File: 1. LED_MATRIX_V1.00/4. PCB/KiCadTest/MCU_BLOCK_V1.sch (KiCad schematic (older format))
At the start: 5 parts, among them U1 ATmega328P-AU, Y1 16 MHz

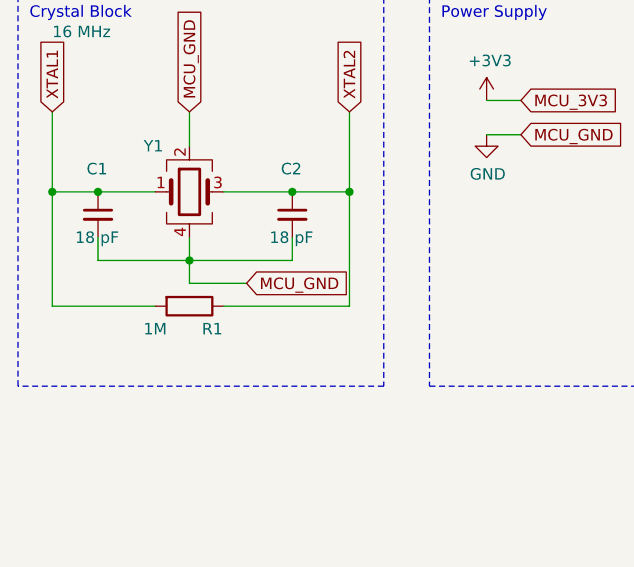
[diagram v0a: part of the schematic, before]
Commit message: Crystal complete_starting reset circuit
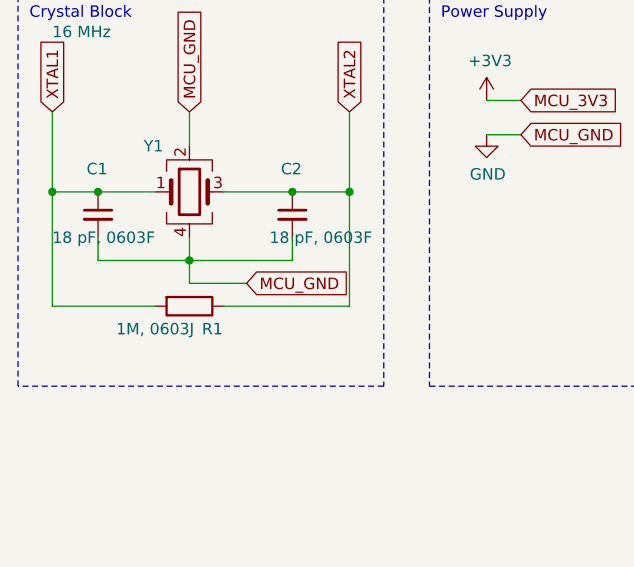
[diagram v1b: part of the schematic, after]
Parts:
- C1, C2: value 18 pF -> 18 pF, 0603F; footprint (none) -> Capacitor_SMD:C_0603_1608Metric
- R1: value 1M -> 1M, 0603J; footprint (none) -> Resistor_SMD:R_0603_1608Metric; Part Number (none) -> CRCW06031M00JKEA
- Y1: Part Number (none) -> TSX-3225 16.0000MF09Z-AC0
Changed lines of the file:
@@
 EESchema Schematic File Version 4
+LIBS:MCU_BLOCK_V1-cache
 EELAYER 29 0
 EELAYER END
@@
 F 2 "Oscillator:Oscillator_SMD_SeikoEpson_SG8002CE-4Pin_3.2x2.5mm_HandSoldering" H 1350 1400 50  0001 C CNN
 F 3 "" H 1350 1400 50  0001 C CNN
+F 4 "TSX-3225 16.0000MF09Z-AC0" H 1350 1400 50  0001 C CNN "Part Number"
 	1    1350 1400
 	1    0    0    -1
@@
 P 1350 1900
 F 0 "R1" V 1450 2000 50  0000 C CNN
-F 1 "1M" V 1450 1750 50  0000 C CNN
-F 2 "" V 1280 1900 50  0001 C CNN
+F 1 "1M, 0603J" V 1450 1750 50  0000 C CNN
+F 2 "Resistor_SMD:R_0603_1608Metric" V 1280 1900 50  0001 C CNN
 F 3 "~" H 1350 1900 50  0001 C CNN
+F 4 "CRCW06031M00JKEA" V 1350 1900 50  0001 C CNN "Part Number"
 	1    1350 1900
 	0    1    1    0
@@
 P 950 1500
 F 0 "C1" H 900 1700 50  0000 L CNN
-F 1 "18 pF" H 850 1400 50  0000 L CNN
-F 2 "" H 950 1500 50  0001 C CNN
+F 1 "18 pF, 0603F" H 750 1400 50  0000 L CNN
+F 2 "Capacitor_SMD:C_0603_1608Metric" H 950 1500 50  0001 C CNN
 F 3 "~" H 950 1500 50  0001 C CNN
 	1    950  1500
@@
 P 1800 1500
 F 0 "C2" H 1750 1700 50  0000 L CNN
-F 1 "18 pF" H 1700 1400 50  0000 L CNN
-F 2 "" H 1800 1500 50  0001 C CNN
+F 1 "18 pF, 0603F" H 1700 1400 50  0000 L CNN
+F 2 "Capacitor_SMD:C_0603_1608Metric" H 1800 1500 50  0001 C CNN
 F 3 "~" H 1800 1500 50  0001 C CNN
 	1    1800 1500

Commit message: Crystal complete_reset in progress
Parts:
- added C3: 0.1 uF, 0603J, Capacitor_SMD:C_0201_0603Metric, symbol Device:C
- added R2: 10 K, 0603J, Resistor_SMD:R_0201_0603Metric, symbol Device:R
- C1, C2: Part Number (none) -> VJ0603A180FXACW1BC
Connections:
- net +3V3: now also R2.1
- net GND: now also C3.2
- net RESET: now reaches U1.29 (~RESET~/PC6)
- net RESET: now also C3.1, R2.2
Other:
- note added: "Reset Block"
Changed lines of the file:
@@
 F 2 "Capacitor_SMD:C_0603_1608Metric" H 950 1500 50  0001 C CNN
 F 3 "~" H 950 1500 50  0001 C CNN
+F 4 "VJ0603A180FXACW1BC" H 950 1500 50  0001 C CNN "Part Number"
 	1    950  1500
 	1    0    0    -1
@@
 P 1800 1500
 F 0 "C2" H 1750 1700 50  0000 L CNN
-F 1 "18 pF, 0603F" H 1700 1400 50  0000 L CNN
+F 1 "18 pF, 0603F" H 1550 1400 50  0000 L CNN
 F 2 "Capacitor_SMD:C_0603_1608Metric" H 1800 1500 50  0001 C CNN
 F 3 "~" H 1800 1500 50  0001 C CNN
+F 4 "VJ0603A180FXACW1BC" H 1800 1500 50  0001 C CNN "Part Number"
 	1    1800 1500
 	1    0    0    -1
@@
 Text GLabel 5550 1850 1    50   Input ~ 0
 MCU_3V3
-Text GLabel 2800 1150 2    50   Input ~ 0
-MCU_GND
 Text GLabel 5550 5200 3    50   Input ~ 0
 MCU_GND
@@
 Wire Wire Line
 	5550 5200 5550 5050
+$Comp
+L Device:R R2
+U 1 1 5D504F89
+P 1200 2800
+F 0 "R2" H 1270 2846 50  0000 L CNN
+F 1 "10 K, 0603J" H 1270 2755 50  0000 L CNN
+F 2 "Resistor_SMD:R_0201_0603Metric" V 1130 2800 50  0001 C CNN
+F 3 "~" H 1200 2800 50  0001 C CNN
+F 4 "" H 1200 2800 50  0001 C CNN "Part Number"
+	1    1200 2800
+	1    0    0    -1
+$EndComp
+$Comp
+L Device:C C3
+U 1 1 5D5066E7
+P 1200 3200
+F 0 "C3" H 1315 3246 50  0000 L CNN
+F 1 "0.1 uF, 0603J" H 1200 3100 50  0000 L CNN
+F 2 "Capacitor_SMD:C_0201_0603Metric" H 1238 3050 50  0001 C CNN
+F 3 "~" H 1200 3200 50  0001 C CNN
+F 4 "" H 1200 3200 50  0001 C CNN "Part Number"
+	1    1200 3200
+	1    0    0    -1
+$EndComp
+Text GLabel 1200 2550 0    50   Input ~ 0
+MCU_3V3
+Text GLabel 2800 1150 2    50   Input ~ 0
+MCU_GND
+Text GLabel 1200 3450 0    50   Input ~ 0
+MCU_GND
+Wire Wire Line
+	1200 2550 1200 2650
+Wire Wire Line
+	1200 2950 1200 3000
+Wire Wire Line
+	1200 3350 1200 3450
+Text GLabel 1350 3000 2    50   Input ~ 0
+RESET
+Wire Wire Line
+	1350 3000 1200 3000
+Connection ~ 1200 3000
+Wire Wire Line
+	1200 3000 1200 3050
+Text GLabel 6350 3850 2    50   Input ~ 0
+RESET
+Wire Wire Line
+	6150 3850 6350 3850
+Wire Notes Line
+	600  3600 1750 3600
+Wire Notes Line
+	1750 3600 1750 2300
+Wire Notes Line
+	1750 2300 600  2300
+Wire Notes Line
+	600  2300 600  3600
+Text Notes 650  2400 0    50   ~ 0
+Reset Block
 $EndSCHEMATC

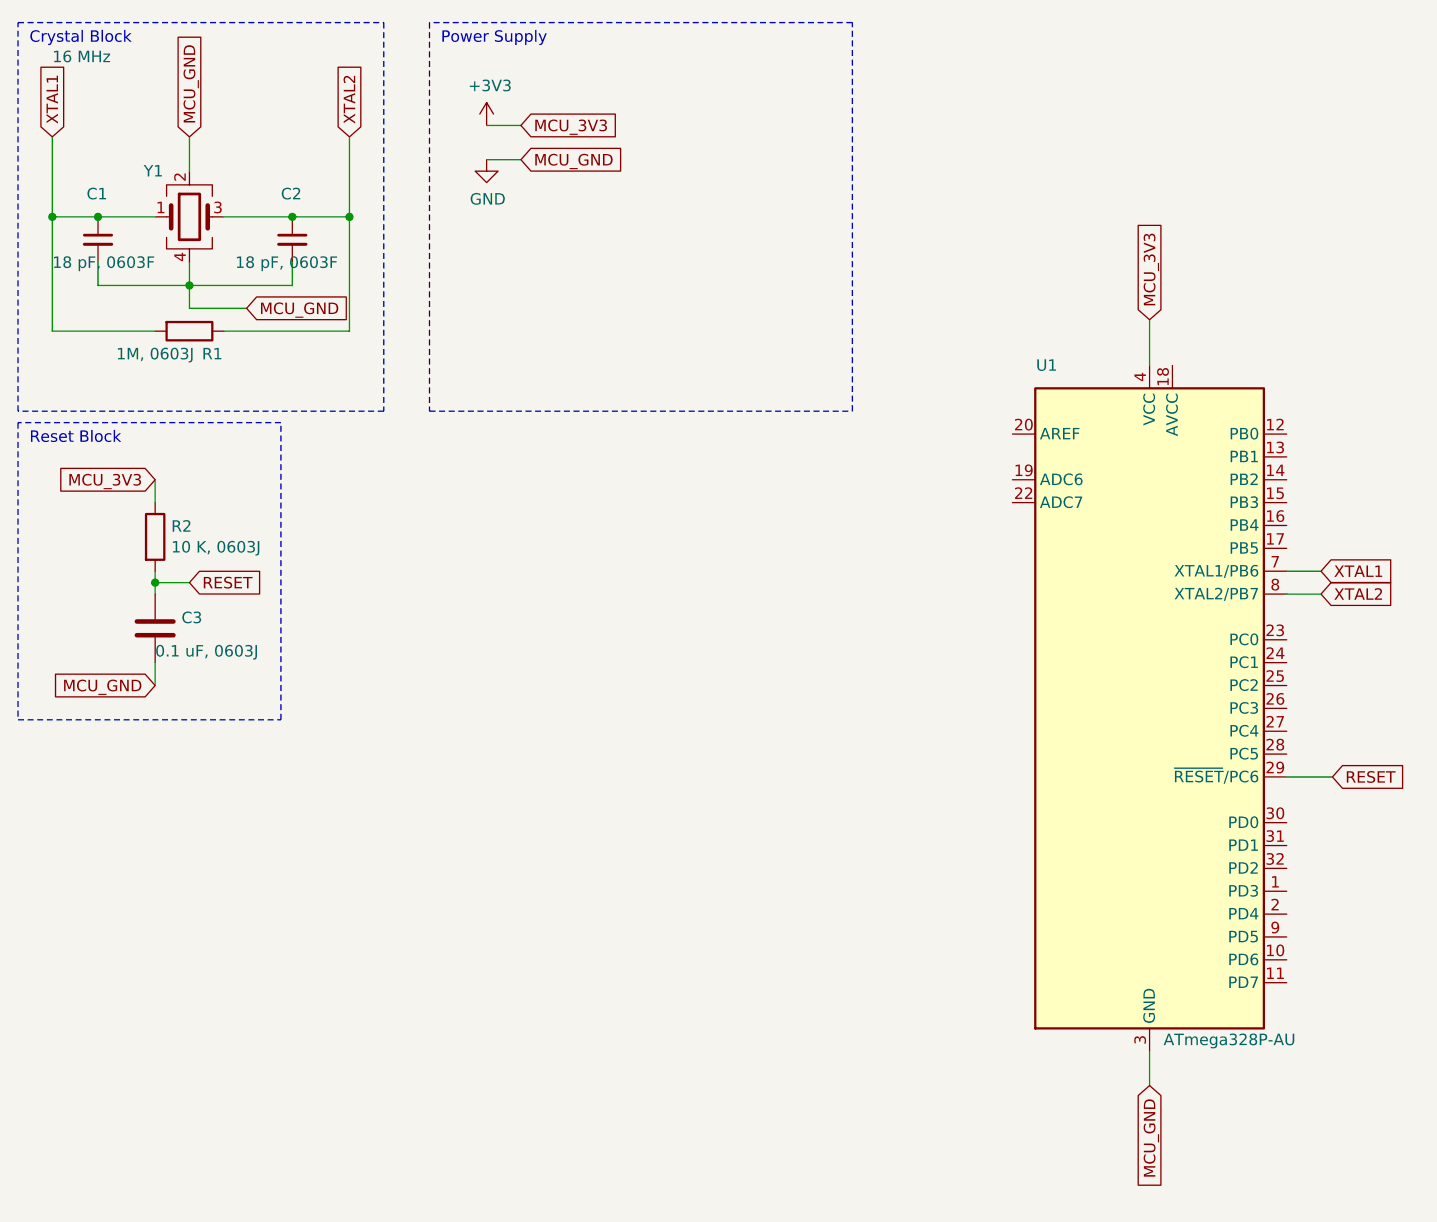
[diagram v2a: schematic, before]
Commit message: Reset Done, UART header added, ISP header added in schematic
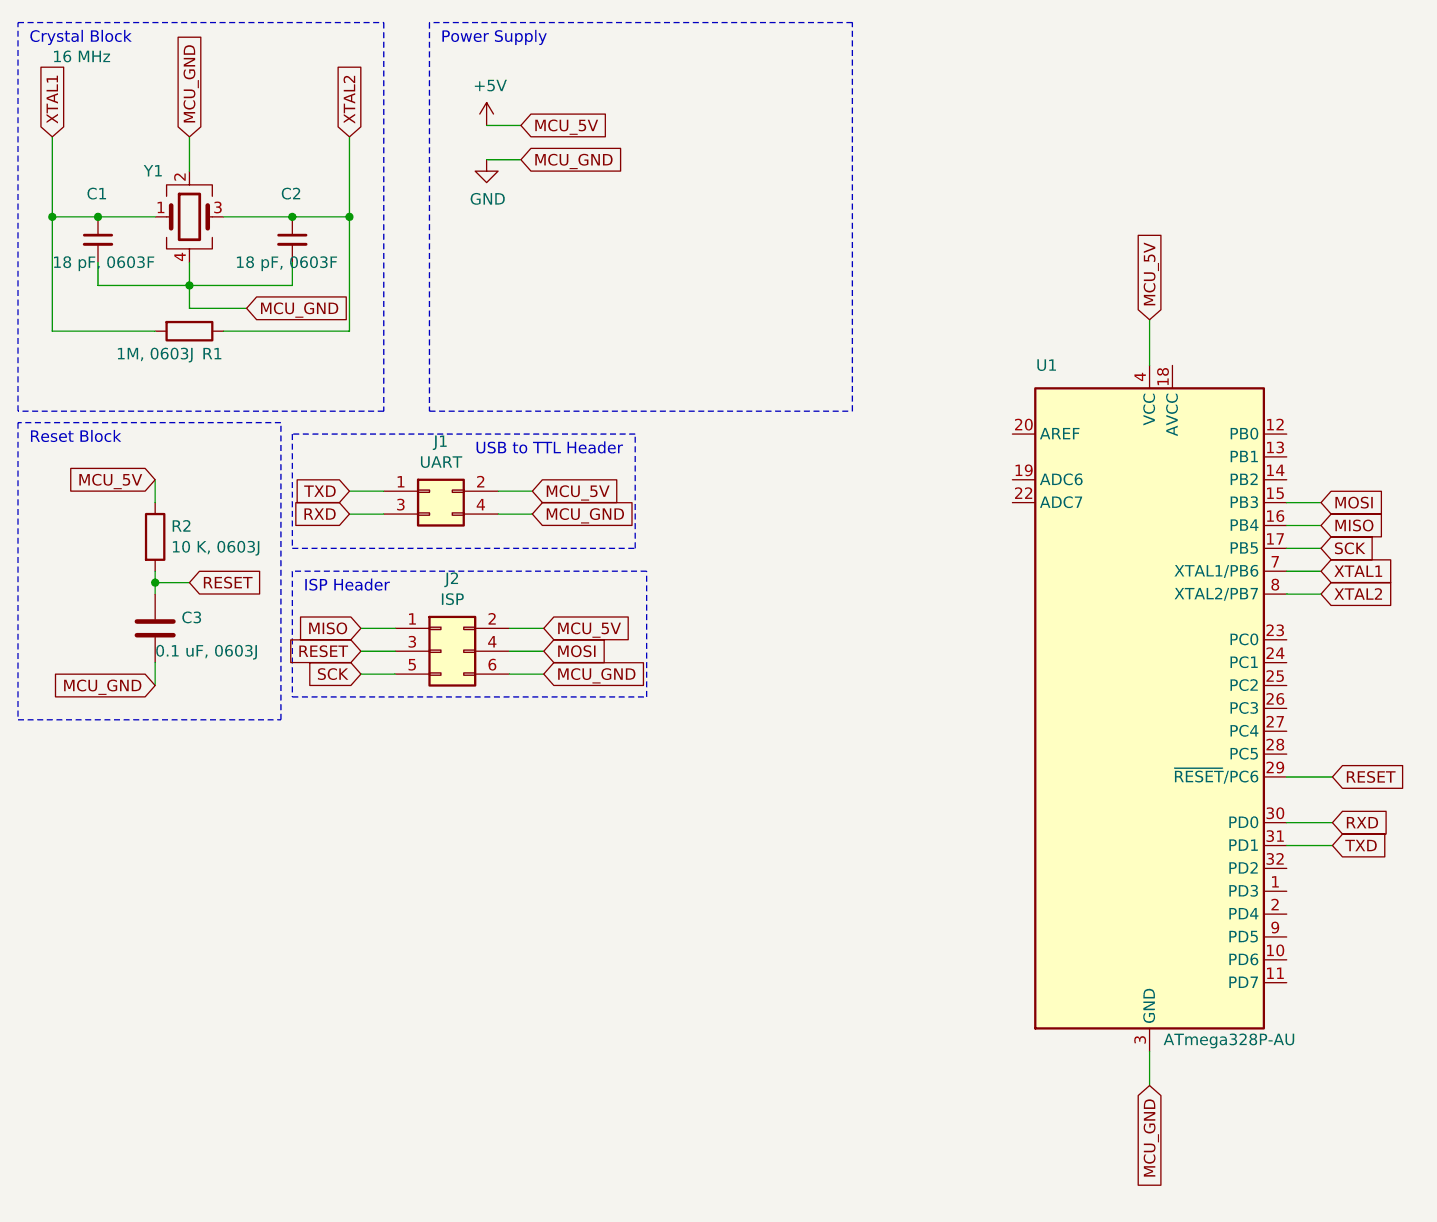
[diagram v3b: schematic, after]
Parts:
- added J1: UART, Connector_PinSocket_2.54mm:PinSocket_2x02_P2.54mm_Vertical, symbol Connector_Generic:Conn_02x02_Odd_Even
- added J2: ISP, Connector_PinSocket_2.54mm:PinSocket_2x03_P2.54mm_Vertical, symbol Connector_Generic:Conn_02x03_Odd_Even
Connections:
- net GND: now also J1.4 (Pin_4), J2.6 (Pin_6)
- net RESET: now also J2.3 (Pin_3)
- net MOSI: now reaches U1.15 (PB3)
- net MOSI: now also J2.4 (Pin_4)
- net MISO: now reaches U1.16 (PB4)
- net MISO: now also J2.1 (Pin_1)
- net SCK: now reaches U1.17 (PB5)
- net SCK: now also J2.5 (Pin_5)
- net RXD: now reaches U1.30 (PD0)
- net RXD: now also J1.3 (Pin_3)
- net TXD: now reaches U1.31 (PD1)
- net TXD: now also J1.1 (Pin_1)
- net +3V3 renamed +5V
- net +5V: now also J1.2 (Pin_2), J2.2 (Pin_2)
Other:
- note added: "ISP Header"
- note added: "USB to TTL Header"
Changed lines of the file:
@@
 	1800 1400 2050 1400
-$Comp
-L power:+3V3 #PWR01
-U 1 1 5D50E48D
-P 2650 1000
-F 0 "#PWR01" H 2650 850 50  0001 C CNN
-F 1 "+3V3" H 2665 1173 50  0000 C CNN
-F 2 "" H 2650 1000 50  0001 C CNN
-F 3 "" H 2650 1000 50  0001 C CNN
-	1    2650 1000
-	1    0    0    -1
-$EndComp
 $Comp
 L power:GND #PWR02
@@
 $EndComp
 Text GLabel 2800 1000 2    50   Input ~ 0
-MCU_3V3
-Wire Wire Line
-	2650 1000 2800 1000
+MCU_5V
 Wire Wire Line
 	2650 1150 2800 1150
@@
 Power Supply
 Text GLabel 5550 1850 1    50   Input ~ 0
-MCU_3V3
+MCU_5V
 Text GLabel 5550 5200 3    50   Input ~ 0
 MCU_GND
@@
 $EndComp
 Text GLabel 1200 2550 0    50   Input ~ 0
-MCU_3V3
+MCU_5V
 Text GLabel 2800 1150 2    50   Input ~ 0
 MCU_GND
@@
 Text Notes 650  2400 0    50   ~ 0
 Reset Block
+$Comp
+L Connector_Generic:Conn_02x02_Odd_Even J1
+U 1 1 5D51A412
+P 2400 2600
+F 0 "J1" H 2450 2817 50  0000 C CNN
+F 1 "UART" H 2450 2726 50  0000 C CNN
+F 2 "Connector_PinSocket_2.54mm:PinSocket_2x02_P2.54mm_Vertical" H 2400 2600 50  0001 C CNN
+F 3 "~" H 2400 2600 50  0001 C CNN
+	1    2400 2600
+	1    0    0    -1
+$EndComp
+$Comp
+L Connector_Generic:Conn_02x03_Odd_Even J2
+U 1 1 5D51B0B6
+P 2450 3300
+F 0 "J2" H 2500 3617 50  0000 C CNN
+F 1 "ISP" H 2500 3526 50  0000 C CNN
+F 2 "Connector_PinSocket_2.54mm:PinSocket_2x03_P2.54mm_Vertical" H 2450 3300 50  0001 C CNN
+F 3 "~" H 2450 3300 50  0001 C CNN
+	1    2450 3300
+	1    0    0    -1
+$EndComp
+Text GLabel 2100 3200 0    50   Input ~ 0
+MISO
+Text GLabel 2100 3300 0    50   Input ~ 0
+RESET
+Text GLabel 2100 3400 0    50   Input ~ 0
+SCK
+Text GLabel 2900 3300 2    50   Input ~ 0
+MOSI
+Text GLabel 2900 3400 2    50   Input ~ 0
+MCU_GND
+Wire Wire Line
+	2100 3200 2250 3200
+Wire Wire Line
+	2250 3300 2100 3300
+Wire Wire Line
+	2100 3400 2250 3400
+Wire Wire Line
+	2750 3200 2900 3200
+Wire Wire Line
+	2750 3300 2900 3300
+Wire Wire Line
+	2750 3400 2900 3400
+Text GLabel 2900 3200 2    50   Input ~ 0
+MCU_5V
+$Comp
+L power:+5V #PWR01
+U 1 1 5D5214D8
+P 2650 1000
+F 0 "#PWR01" H 2650 850 50  0001 C CNN
+F 1 "+5V" H 2665 1173 50  0000 C CNN
+F 2 "" H 2650 1000 50  0001 C CNN
+F 3 "" H 2650 1000 50  0001 C CNN
+	1    2650 1000
+	1    0    0    -1
+$EndComp
+Wire Wire Line
+	2650 1000 2800 1000
+Text GLabel 6300 2650 2    50   Input ~ 0
+MOSI
+Text GLabel 6300 2750 2    50   Input ~ 0
+MISO
+Text GLabel 6300 2850 2    50   Input ~ 0
+SCK
+Wire Wire Line
+	6300 2850 6150 2850
+Wire Wire Line
+	6300 2750 6150 2750
+Wire Wire Line
+	6300 2650 6150 2650
+Text GLabel 2850 2600 2    50   Input ~ 0
+MCU_5V
+Text GLabel 2850 2700 2    50   Input ~ 0
+MCU_GND
+Text GLabel 2050 2600 0    50   Input ~ 0
+TXD
+Text GLabel 2050 2700 0    50   Input ~ 0
+RXD
+Wire Wire Line
+	2050 2600 2200 2600
+Wire Wire Line
+	2200 2700 2050 2700
+Wire Wire Line
+	2700 2600 2850 2600
+Wire Wire Line
+	2850 2700 2700 2700
+Text GLabel 6350 4150 2    50   Input ~ 0
+TXD
+Text GLabel 6350 4050 2    50   Input ~ 0
+RXD
+Wire Wire Line
+	6350 4050 6150 4050
+Wire Wire Line
+	6150 4150 6350 4150
+Wire Notes Line
+	1800 2350 1800 2850
+Wire Notes Line
+	1800 2850 3300 2850
+Wire Notes Line
+	3300 2850 3300 2350
+Wire Notes Line
+	3300 2350 1800 2350
+Wire Notes Line
+	1800 3500 3350 3500
+Wire Notes Line
+	3350 3500 3350 2950
+Wire Notes Line
+	3350 2950 1800 2950
+Wire Notes Line
+	1800 2950 1800 3500
+Text Notes 2600 2450 0    50   ~ 0
+USB to TTL Header
+Text Notes 1850 3050 0    50   ~ 0
+ISP Header
 $EndSCHEMATC
